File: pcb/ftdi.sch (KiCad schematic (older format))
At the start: 44 parts, among them Q3 AO3401A, U2 FT2232HL, U3 M93C46-WMN6TP, U4 MC74VHC1GT04DFT1, U5 74AHC125BQ,115, Y1 ECS-120-18-33-JEM-TR

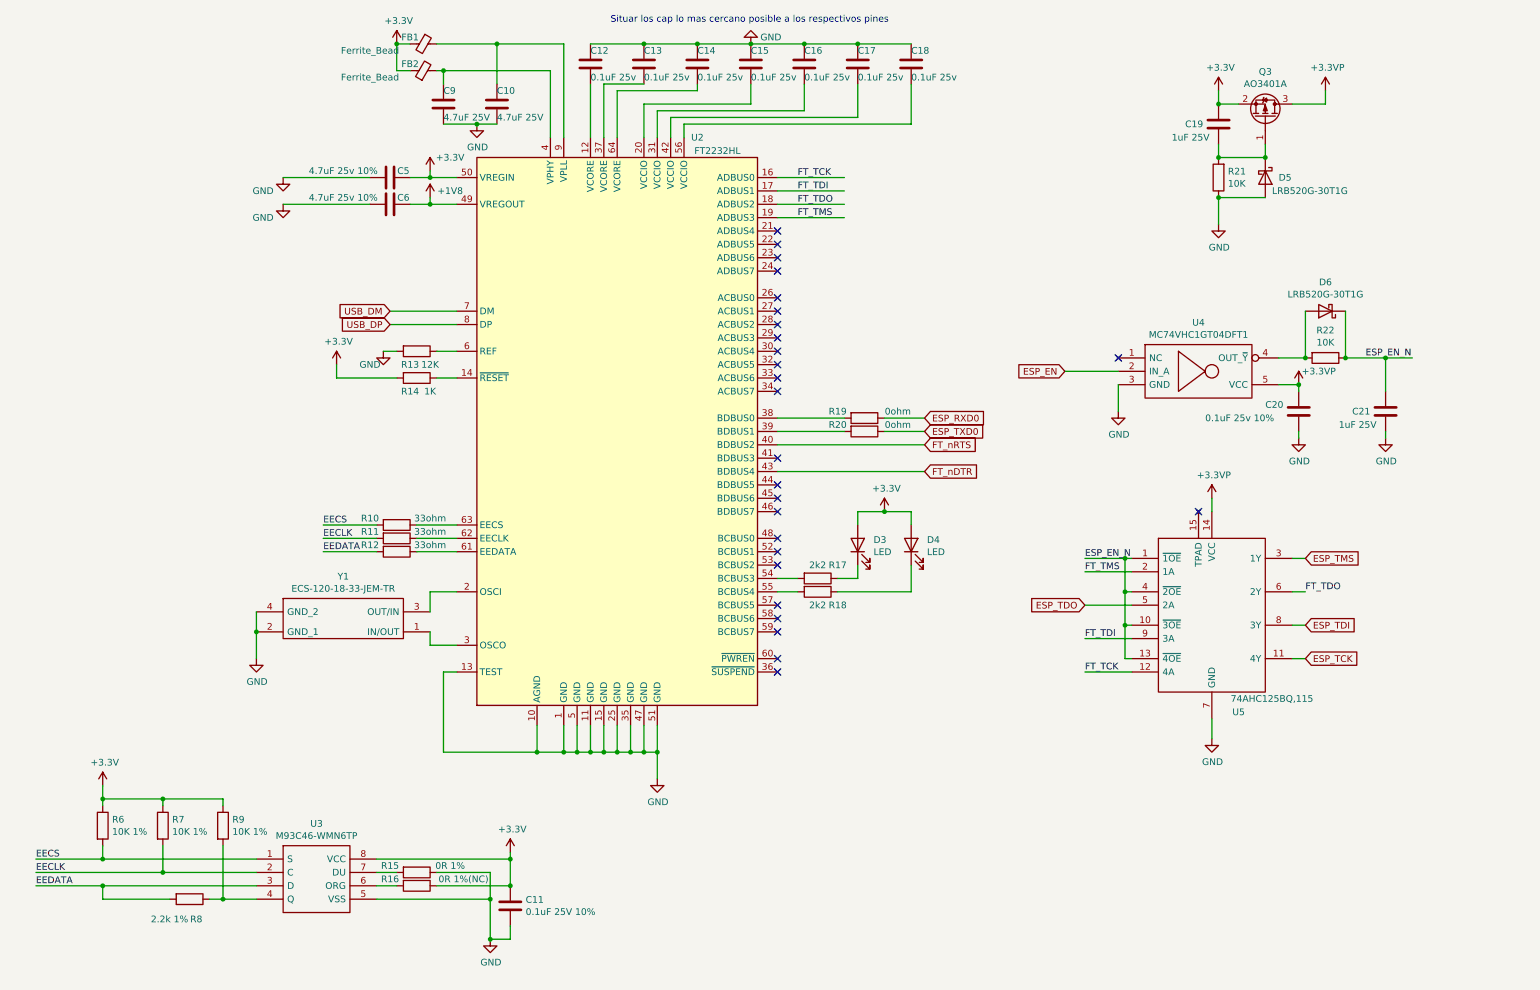
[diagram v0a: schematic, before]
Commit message: correcciones al esquematico y avances en posicionamiento de pcb
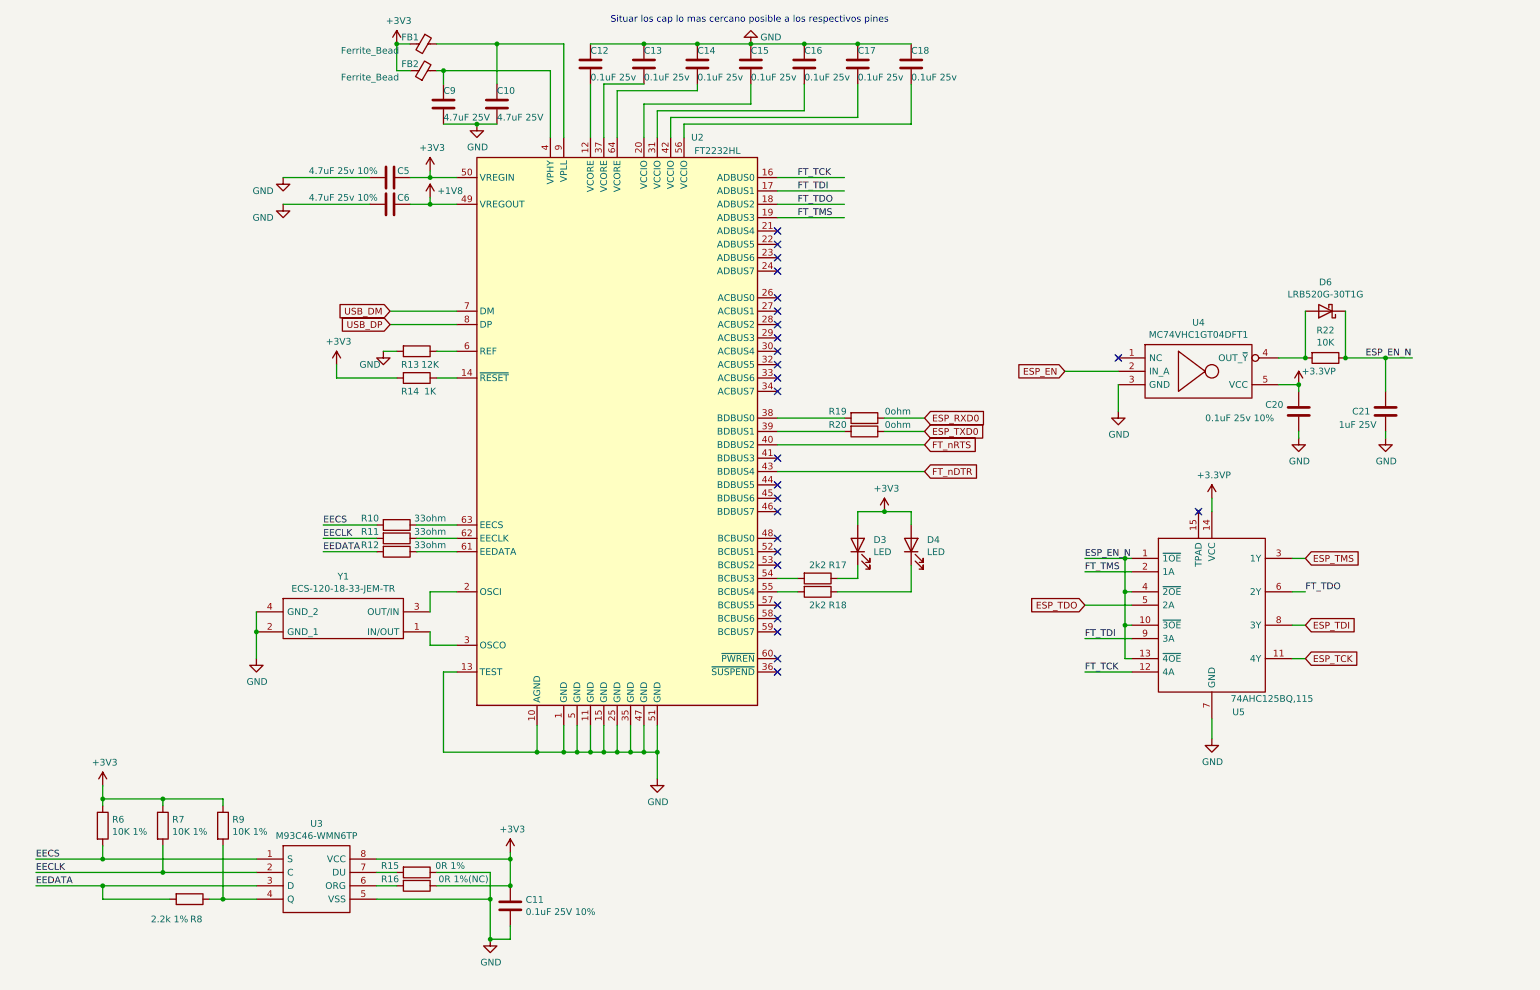
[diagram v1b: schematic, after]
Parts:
- removed C19: 1uF 25V, Capacitor_SMD:C_0603_1608Metric, symbol Device:C
- removed D5: LRB520G-30T1G, Diode_SMD:D_0603_1608Metric, symbol Device:D_Schottky
- removed Q3: AO3401A, Package_TO_SOT_SMD:SOT-23, symbol Transistor_FET:AO3401A
- removed R21: 10K, Resistor_SMD:R_0603_1608Metric, symbol Device:R
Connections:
- net labels added: +3V3
- net labels removed: +3.3V
- wire segments 175 -> 166
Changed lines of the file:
@@
 	4500 6050 4700 6050
-$Comp
-L power:+3.3V #PWR?
-U 1 1 60E78B2D
-P 3700 1700
-AR Path="/60E78B2D" Ref="#PWR?"  Part="1"
-AR Path="/60E64650/60E78B2D" Ref="#PWR0111"  Part="1"
-F 0 "#PWR0111" H 3700 1550 50  0001 C CNN
-F 1 "+3.3V" H 3850 1800 50  0000 C CNN
-F 2 "" H 3700 1700 50  0001 C CNN
-F 3 "" H 3700 1700 50  0001 C CNN
-	1    3700 1700
-	1    0    0    -1
-$EndComp
 $Comp
 L power:+1V8 #PWR?
@@
 Wire Wire Line
 	2150 7150 2400 7150
-$Comp
-L power:+3.3V #PWR011
-U 1 1 60E89B08
-P 1250 6300
-F 0 "#PWR011" H 1250 6150 50  0001 C CNN
-F 1 "+3.3V" H 1265 6473 50  0000 C CNN
-F 2 "" H 1250 6300 50  0001 C CNN
-F 3 "" H 1250 6300 50  0001 C CNN
-	1    1250 6300
-	1    0    0    -1
-$EndComp
 Wire Wire Line
 	1250 6300 1250 6400
@@
 Wire Wire Line
 	3450 7050 3300 7050
-$Comp
-L power:+3.3V #PWR018
-U 1 1 60E93B6B
-P 4300 6800
-F 0 "#PWR018" H 4300 6650 50  0001 C CNN
-F 1 "+3.3V" H 4315 6973 50  0000 C CNN
-F 2 "" H 4300 6800 50  0001 C CNN
-F 3 "" H 4300 6800 50  0001 C CNN
-	1    4300 6800
-	1    0    0    -1
-$EndComp
 Wire Wire Line
 	4300 6850 4300 6800
@@
 Text Label 10700 3100 0    50   ~ 0
 ESP_EN_N
-$Comp
-L Device:R R21
-U 1 1 60F3FD18
-P 9600 1750
-F 0 "R21" H 9530 1704 50  0000 R CNN
-F 1 "10K" H 9530 1795 50  0000 R CNN
-F 2 "Resistor_SMD:R_0603_1608Metric" V 9530 1750 50  0001 C CNN
-F 3 "~" H 9600 1750 50  0001 C CNN
-	1    9600 1750
-	-1   0    0    1
-$EndComp
-$Comp
-L Device:D_Schottky D5
-U 1 1 60F3FD1E
-P 9950 1750
-F 0 "D5" V 9950 1850 50  0000 L CNN
-F 1 "LRB520G-30T1G" V 10050 1800 50  0000 L CNN
-F 2 "Diode_SMD:D_0603_1608Metric" H 9950 1750 50  0001 C CNN
-F 3 "~" H 9950 1750 50  0001 C CNN
-	1    9950 1750
-	0    1    1    0
-$EndComp
-$Comp
-L Device:C C19
-U 1 1 60F3FD29
-P 9600 1350
-F 0 "C19" H 9350 1350 50  0000 L CNN
-F 1 "1uF 25V" H 9250 1250 50  0000 L CNN
-F 2 "Capacitor_SMD:C_0603_1608Metric" H 9638 1200 50  0001 C CNN
-F 3 "~" H 9600 1350 50  0001 C CNN
-	1    9600 1350
-	1    0    0    -1
-$EndComp
-$Comp
-L power:GND #PWR025
-U 1 1 60F3FD2F
-P 9600 2100
-F 0 "#PWR025" H 9600 1850 50  0001 C CNN
-F 1 "GND" H 9605 1927 50  0000 C CNN
-F 2 "" H 9600 2100 50  0001 C CNN
-F 3 "" H 9600 2100 50  0001 C CNN
-	1    9600 2100
-	1    0    0    -1
-$EndComp
-Wire Wire Line
-	9950 1900 9600 1900
-Wire Wire Line
-	9600 1900 9600 2100
-Connection ~ 9600 1900
-Wire Wire Line
-	9600 1500 9600 1600
-Connection ~ 9600 1600
-$Comp
-L Transistor_FET:AO3401A Q3
-U 1 1 60F4DEE9
-P 9950 1300
-F 0 "Q3" V 10292 1300 50  0000 C CNN
-F 1 "AO3401A" V 10201 1300 50  0000 C CNN
-F 2 "Package_TO_SOT_SMD:SOT-23" H 10150 1225 50  0001 L CIN
-F 3 "http://www.aosmd.com/pdfs/datasheet/AO3401A.pdf" H 9950 1300 50  0001 L CNN
-	1    9950 1300
-	0    1    -1   0
-$EndComp
-Wire Wire Line
-	9950 1500 9950 1600
-Wire Wire Line
-	9750 1200 9600 1200
-Wire Wire Line
-	9600 1200 9600 1100
-Connection ~ 9600 1200
-Wire Wire Line
-	10150 1200 10400 1200
-Wire Wire Line
-	10400 1200 10400 1100
-$Comp
-L power:+3.3VP #PWR028
-U 1 1 60F5B025
-P 10400 1100
-F 0 "#PWR028" H 10550 1050 50  0001 C CNN
-F 1 "+3.3VP" H 10415 1273 50  0000 C CNN
-F 2 "" H 10400 1100 50  0001 C CNN
-F 3 "" H 10400 1100 50  0001 C CNN
-	1    10400 1100
-	1    0    0    -1
-$EndComp
-$Comp
-L power:+3.3V #PWR024
-U 1 1 60F5BA66
-P 9600 1100
-F 0 "#PWR024" H 9600 950 50  0001 C CNN
-F 1 "+3.3V" H 9615 1273 50  0000 C CNN
-F 2 "" H 9600 1100 50  0001 C CNN
-F 3 "" H 9600 1100 50  0001 C CNN
-	1    9600 1100
-	1    0    0    -1
-$EndComp
-Connection ~ 9950 1600
-Wire Wire Line
-	9600 1600 9950 1600
 Wire Wire Line
 	6300 1750 6800 1750
@@
 Wire Wire Line
 	6750 4850 7300 4850
-$Comp
-L power:+3.3V #PWR020
-U 1 1 60FEEF06
-P 7100 4250
-F 0 "#PWR020" H 7100 4100 50  0001 C CNN
-F 1 "+3.3V" H 7115 4423 50  0000 C CNN
-F 2 "" H 7100 4250 50  0001 C CNN
-F 3 "" H 7100 4250 50  0001 C CNN
-	1    7100 4250
-	1    0    0    -1
-$EndComp
 Wire Wire Line
 	6900 4350 6900 4250
 Wire Wire Line
-	6900 4250 7100 4250
-Wire Wire Line
-	7100 4250 7300 4250
-Wire Wire Line
 	7300 4250 7300 4350
-Connection ~ 7100 4250
 $Comp
 L Device:R R19
@@
 Wire Wire Line
 	3000 3250 3000 3150
-$Comp
-L power:+3.3V #PWR013
-U 1 1 61020218
-P 3000 3150
-F 0 "#PWR013" H 3000 3000 50  0001 C CNN
-F 1 "+3.3V" H 3015 3323 50  0000 C CNN
-F 2 "" H 3000 3150 50  0001 C CNN
-F 3 "" H 3000 3150 50  0001 C CNN
-	1    3000 3150
-	1    0    0    -1
-$EndComp
 $Comp
 L Device:R R10
@@
 Wire Wire Line
 	4700 750  4200 750
-$Comp
-L power:+3.3V #PWR015
-U 1 1 60FA900A
-P 3450 750
-F 0 "#PWR015" H 3450 600 50  0001 C CNN
-F 1 "+3.3V" H 3465 923 50  0000 C CNN
-F 2 "" H 3450 750 50  0001 C CNN
-F 3 "" H 3450 750 50  0001 C CNN
-	1    3450 750
-	1    0    0    -1
-$EndComp
 Wire Wire Line
 	3450 950  3450 750
@@
 Text GLabel 3400 2850 0    50   Input ~ 0
 USB_DP
+Wire Wire Line
+	3550 750  3450 750
+Wire Wire Line
+	3550 950  3450 950
+Wire Wire Line
+	3800 1350 4050 1350
+$Comp
+L power:+3V3 #PWR?
+U 1 1 6124C8B5
+P 7100 4250
+F 0 "#PWR?" H 7100 4100 50  0001 C CNN
+F 1 "+3V3" H 7115 4423 50  0000 C CNN
+F 2 "" H 7100 4250 50  0001 C CNN
+F 3 "" H 7100 4250 50  0001 C CNN
+	1    7100 4250
+	1    0    0    -1
+$EndComp
+Wire Wire Line
+	6900 4250 7100 4250
+Connection ~ 7100 4250
+Wire Wire Line
+	7100 4250 7300 4250
+$Comp
+L power:+3V3 #PWR?
+U 1 1 6124D8E8
+P 1250 6300
+F 0 "#PWR?" H 1250 6150 50  0001 C CNN
+F 1 "+3V3" H 1265 6473 50  0000 C CNN
+F 2 "" H 1250 6300 50  0001 C CNN
+F 3 "" H 1250 6300 50  0001 C CNN
+	1    1250 6300
+	1    0    0    -1
+$EndComp
+$Comp
+L power:+3V3 #PWR?
+U 1 1 6124EBB5
+P 4300 6800
+F 0 "#PWR?" H 4300 6650 50  0001 C CNN
+F 1 "+3V3" H 4315 6973 50  0000 C CNN
+F 2 "" H 4300 6800 50  0001 C CNN
+F 3 "" H 4300 6800 50  0001 C CNN
+	1    4300 6800
+	1    0    0    -1
+$EndComp
+$Comp
+L power:+3V3 #PWR?
+U 1 1 612505CF
+P 3000 3150
+F 0 "#PWR?" H 3000 3000 50  0001 C CNN
+F 1 "+3V3" H 3015 3323 50  0000 C CNN
+F 2 "" H 3000 3150 50  0001 C CNN
+F 3 "" H 3000 3150 50  0001 C CNN
+	1    3000 3150
+	1    0    0    -1
+$EndComp
+$Comp
+L power:+3V3 #PWR?
+U 1 1 612514BC
+P 3450 750
+F 0 "#PWR?" H 3450 600 50  0001 C CNN
+F 1 "+3V3" H 3465 923 50  0000 C CNN
+F 2 "" H 3450 750 50  0001 C CNN
+F 3 "" H 3450 750 50  0001 C CNN
+	1    3450 750
+	1    0    0    -1
+$EndComp
+$Comp
+L power:+3V3 #PWR?
+U 1 1 6125203A
+P 3700 1700
+F 0 "#PWR?" H 3700 1550 50  0001 C CNN
+F 1 "+3V3" H 3715 1873 50  0000 C CNN
+F 2 "" H 3700 1700 50  0001 C CNN
+F 3 "" H 3700 1700 50  0001 C CNN
+	1    3700 1700
+	1    0    0    -1
+$EndComp
 Connection ~ 3450 750
-Wire Wire Line
-	3550 750  3450 750
-Wire Wire Line
-	3550 950  3450 950
-Wire Wire Line
-	3800 1350 4050 1350
 $EndSCHEMATC

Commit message: - Rpimer propuesta posicionamiento
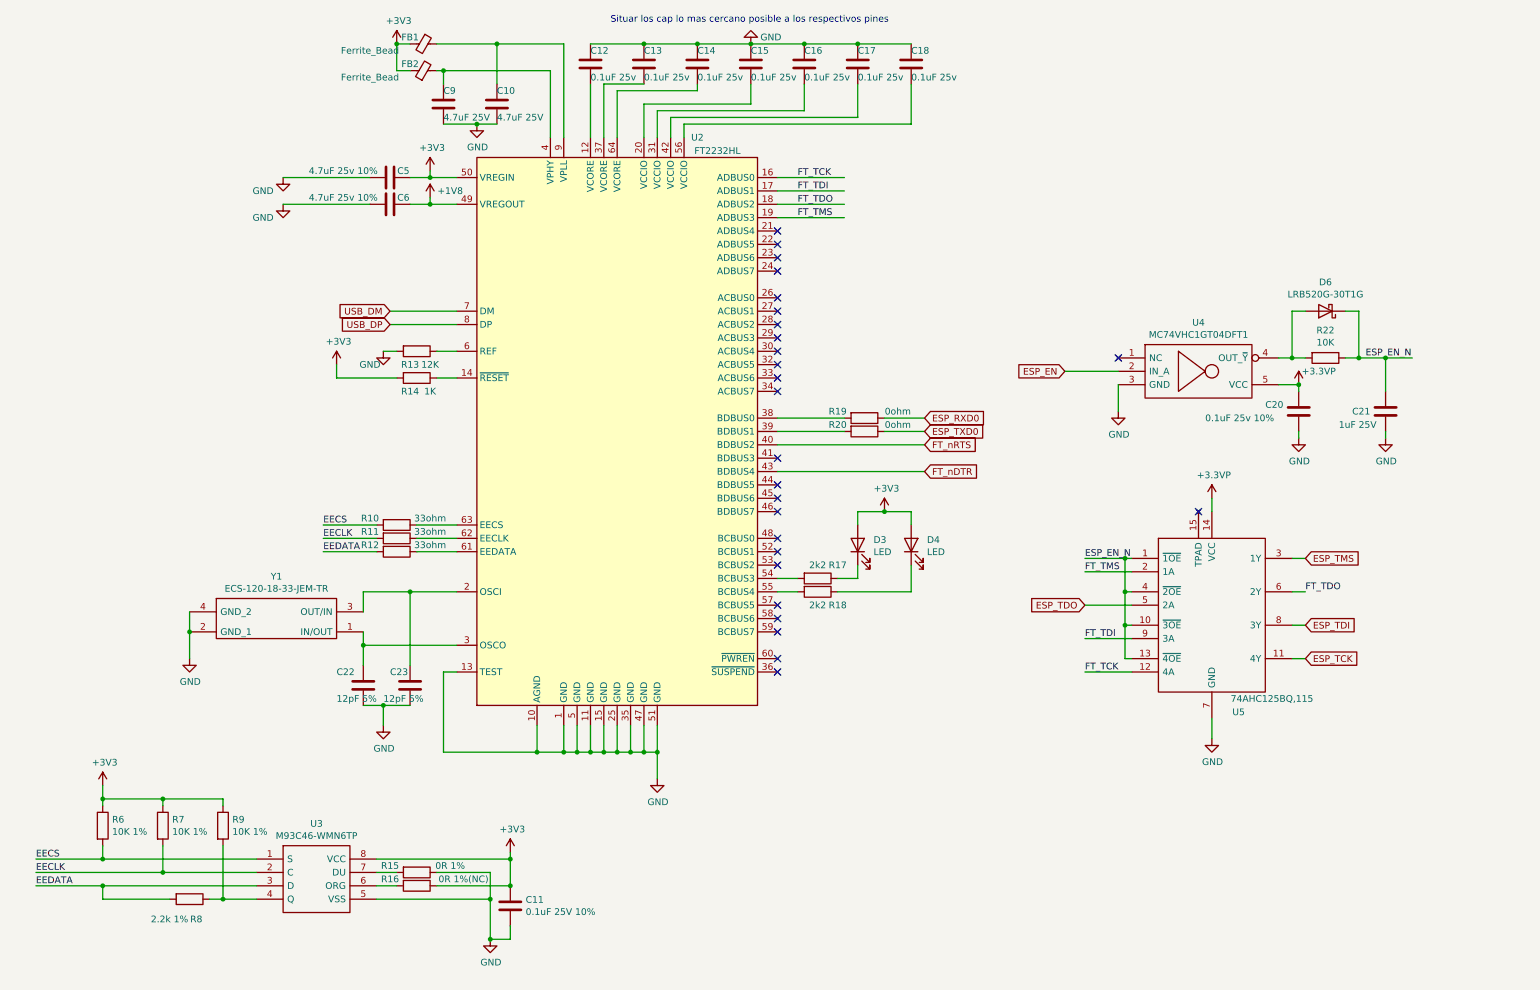
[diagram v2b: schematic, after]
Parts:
- added C22, C23: 12pF 5%, Capacitor_SMD:C_0603_1608Metric, symbol Device:C
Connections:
- wire segments 166 -> 176
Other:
- moved on the sheet: Y1
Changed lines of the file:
@@
 NoConn ~ 8850 3100
 Wire Wire Line
-	10050 3100 10250 3100
+	10050 3100 10150 3100
 $Comp
 L Device:R R22
@@
 $EndComp
 Wire Wire Line
-	10550 2750 10550 3100
-Wire Wire Line
-	10250 3100 10250 2750
-Connection ~ 10250 3100
-Wire Wire Line
-	10550 3100 10850 3100
-Connection ~ 10550 3100
+	10550 3100 10650 3100
 $Comp
 L Device:C C21
@@
 L SamacSys_Parts:ECS-120-18-33-JEM-TR Y1
 U 1 1 60F68BB3
-P 2400 5000
-F 0 "Y1" H 3050 5265 50  0000 C CNN
-F 1 "ECS-120-18-33-JEM-TR" H 3050 5174 50  0000 C CNN
-F 2 "Crystal:Crystal_SMD_0603-4Pin_6.0x3.5mm" H 3550 5100 50  0001 L CNN
-F 3 "https://componentsearchengine.com/Datasheets/1/ECS-120-18-33-JEM-TR.pdf" H 3550 5000 50  0001 L CNN
-F 4 "Crystals 12MHz 20ppm 18pF -20C +70C" H 3550 4900 50  0001 L CNN "Description"
-F 5 "0.8" H 3550 4800 50  0001 L CNN "Height"
-F 6 "520-120-18-33-JEMT" H 3550 4700 50  0001 L CNN "Mouser Part Number"
-F 7 "https://www.mouser.com/Search/Refine.aspx?Keyword=520-120-18-33-JEMT" H 3550 4600 50  0001 L CNN "Mouser Price/Stock"
-F 8 "ECS" H 3550 4500 50  0001 L CNN "Manufacturer_Name"
-F 9 "ECS-120-18-33-JEM-TR" H 3550 4400 50  0001 L CNN "Manufacturer_Part_Number"
-	1    2400 5000
+P 1900 5000
+F 0 "Y1" H 2550 5265 50  0000 C CNN
+F 1 "ECS-120-18-33-JEM-TR" H 2550 5174 50  0000 C CNN
+F 2 "Crystal:Crystal_SMD_0603-4Pin_6.0x3.5mm" H 3050 5100 50  0001 L CNN
+F 3 "https://componentsearchengine.com/Datasheets/1/ECS-120-18-33-JEM-TR.pdf" H 3050 5000 50  0001 L CNN
+F 4 "Crystals 12MHz 20ppm 18pF -20C +70C" H 3050 4900 50  0001 L CNN "Description"
+F 5 "0.8" H 3050 4800 50  0001 L CNN "Height"
+F 6 "520-120-18-33-JEMT" H 3050 4700 50  0001 L CNN "Mouser Part Number"
+F 7 "https://www.mouser.com/Search/Refine.aspx?Keyword=520-120-18-33-JEMT" H 3050 4600 50  0001 L CNN "Mouser Price/Stock"
+F 8 "ECS" H 3050 4500 50  0001 L CNN "Manufacturer_Name"
+F 9 "ECS-120-18-33-JEM-TR" H 3050 4400 50  0001 L CNN "Manufacturer_Part_Number"
+	1    1900 5000
 	1    0    0    -1
 $EndComp
@@
 L power:GND #PWR012
 U 1 1 60F69A25
-P 2400 5350
-F 0 "#PWR012" H 2400 5100 50  0001 C CNN
-F 1 "GND" H 2405 5177 50  0000 C CNN
-F 2 "" H 2400 5350 50  0001 C CNN
-F 3 "" H 2400 5350 50  0001 C CNN
-	1    2400 5350
-	1    0    0    -1
-$EndComp
-Wire Wire Line
-	2400 5000 2400 5150
-Wire Wire Line
-	2400 5350 2400 5150
-Connection ~ 2400 5150
-Wire Wire Line
-	3700 5000 3700 4850
-Wire Wire Line
-	3700 4850 3900 4850
-Wire Wire Line
-	3900 5250 3700 5250
-Wire Wire Line
-	3700 5250 3700 5150
+P 1900 5350
+F 0 "#PWR012" H 1900 5100 50  0001 C CNN
+F 1 "GND" H 1905 5177 50  0000 C CNN
+F 2 "" H 1900 5350 50  0001 C CNN
+F 3 "" H 1900 5350 50  0001 C CNN
+	1    1900 5350
+	1    0    0    -1
+$EndComp
+Wire Wire Line
+	1900 5000 1900 5150
+Wire Wire Line
+	1900 5350 1900 5150
+Connection ~ 1900 5150
+Wire Wire Line
+	3200 5000 3200 4850
+Wire Wire Line
+	3200 4850 3550 4850
+Wire Wire Line
+	3900 5250 3200 5250
+Wire Wire Line
+	3200 5250 3200 5150
 $Comp
 L Device:Ferrite_Bead_Small FB1
@@
 	3800 1350 4050 1350
 $Comp
-L power:+3V3 #PWR?
+L power:+3V3 #PWR032
 U 1 1 6124C8B5
 P 7100 4250
-F 0 "#PWR?" H 7100 4100 50  0001 C CNN
+F 0 "#PWR032" H 7100 4100 50  0001 C CNN
 F 1 "+3V3" H 7115 4423 50  0000 C CNN
 F 2 "" H 7100 4250 50  0001 C CNN
@@
 	7100 4250 7300 4250
 $Comp
-L power:+3V3 #PWR?
+L power:+3V3 #PWR011
 U 1 1 6124D8E8
 P 1250 6300
-F 0 "#PWR?" H 1250 6150 50  0001 C CNN
+F 0 "#PWR011" H 1250 6150 50  0001 C CNN
 F 1 "+3V3" H 1265 6473 50  0000 C CNN
 F 2 "" H 1250 6300 50  0001 C CNN
@@
 $EndComp
 $Comp
-L power:+3V3 #PWR?
+L power:+3V3 #PWR028
 U 1 1 6124EBB5
 P 4300 6800
-F 0 "#PWR?" H 4300 6650 50  0001 C CNN
+F 0 "#PWR028" H 4300 6650 50  0001 C CNN
 F 1 "+3V3" H 4315 6973 50  0000 C CNN
 F 2 "" H 4300 6800 50  0001 C CNN
@@
 $EndComp
 $Comp
-L power:+3V3 #PWR?
+L power:+3V3 #PWR013
 U 1 1 612505CF
 P 3000 3150
-F 0 "#PWR?" H 3000 3000 50  0001 C CNN
+F 0 "#PWR013" H 3000 3000 50  0001 C CNN
 F 1 "+3V3" H 3015 3323 50  0000 C CNN
 F 2 "" H 3000 3150 50  0001 C CNN
@@
 $EndComp
 $Comp
-L power:+3V3 #PWR?
+L power:+3V3 #PWR018
 U 1 1 612514BC
 P 3450 750
-F 0 "#PWR?" H 3450 600 50  0001 C CNN
+F 0 "#PWR018" H 3450 600 50  0001 C CNN
 F 1 "+3V3" H 3465 923 50  0000 C CNN
 F 2 "" H 3450 750 50  0001 C CNN
@@
 $EndComp
 $Comp
-L power:+3V3 #PWR?
+L power:+3V3 #PWR020
 U 1 1 6125203A
 P 3700 1700
-F 0 "#PWR?" H 3700 1550 50  0001 C CNN
+F 0 "#PWR020" H 3700 1550 50  0001 C CNN
 F 1 "+3V3" H 3715 1873 50  0000 C CNN
 F 2 "" H 3700 1700 50  0001 C CNN
@@
 $EndComp
 Connection ~ 3450 750
+$Comp
+L Device:C C22
+U 1 1 611D3A87
+P 3200 5550
+F 0 "C22" H 3000 5650 50  0000 L CNN
+F 1 "12pF 5%" H 3000 5450 50  0000 L CNN
+F 2 "Capacitor_SMD:C_0603_1608Metric" H 3238 5400 50  0001 C CNN
+F 3 "~" H 3200 5550 50  0001 C CNN
+	1    3200 5550
+	1    0    0    -1
+$EndComp
+$Comp
+L Device:C C23
+U 1 1 611D57D3
+P 3550 5550
+F 0 "C23" H 3400 5650 50  0000 L CNN
+F 1 "12pF 5%" H 3350 5450 50  0000 L CNN
+F 2 "Capacitor_SMD:C_0603_1608Metric" H 3588 5400 50  0001 C CNN
+F 3 "~" H 3550 5550 50  0001 C CNN
+	1    3550 5550
+	1    0    0    -1
+$EndComp
+$Comp
+L power:GND #PWR015
+U 1 1 611D5DE1
+P 3350 5850
+F 0 "#PWR015" H 3350 5600 50  0001 C CNN
+F 1 "GND" H 3355 5677 50  0000 C CNN
+F 2 "" H 3350 5850 50  0001 C CNN
+F 3 "" H 3350 5850 50  0001 C CNN
+	1    3350 5850
+	1    0    0    -1
+$EndComp
+Wire Wire Line
+	3200 5400 3200 5250
+Connection ~ 3200 5250
+Wire Wire Line
+	3550 5400 3550 4850
+Connection ~ 3550 4850
+Wire Wire Line
+	3550 4850 3900 4850
+Wire Wire Line
+	3200 5700 3350 5700
+Wire Wire Line
+	3350 5850 3350 5700
+Connection ~ 3350 5700
+Wire Wire Line
+	3350 5700 3550 5700
+Wire Wire Line
+	10150 3100 10150 2750
+Wire Wire Line
+	10150 2750 10250 2750
+Connection ~ 10150 3100
+Wire Wire Line
+	10150 3100 10250 3100
+Wire Wire Line
+	10550 2750 10650 2750
+Wire Wire Line
+	10650 2750 10650 3100
+Connection ~ 10650 3100
+Wire Wire Line
+	10650 3100 10850 3100
 $EndSCHEMATC
